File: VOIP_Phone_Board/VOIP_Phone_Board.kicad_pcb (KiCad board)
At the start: 2 copper layers, 65 x 56 mm, 25 parts, among them J1 69253-002LF, P1 Conn_02x20_Odd_Even, U1 PCM5102

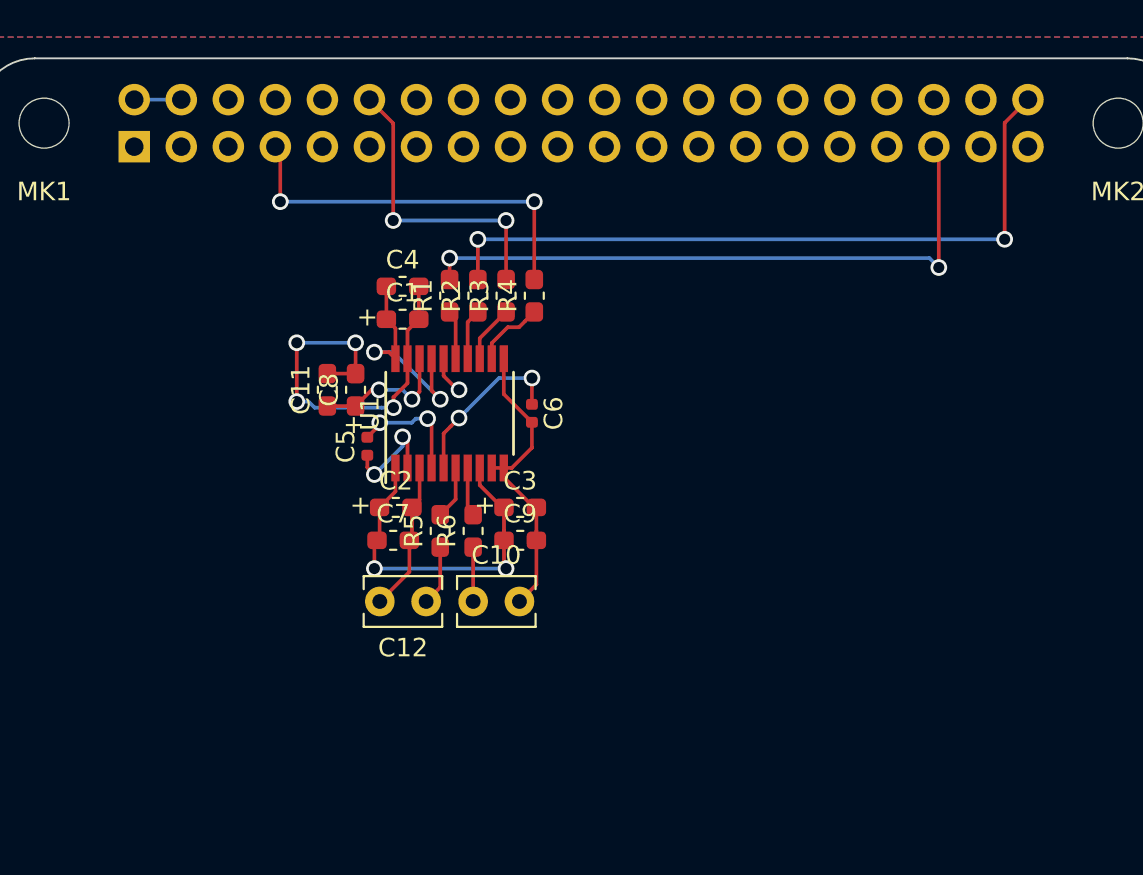
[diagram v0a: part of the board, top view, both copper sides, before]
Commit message: Completed audio input section.
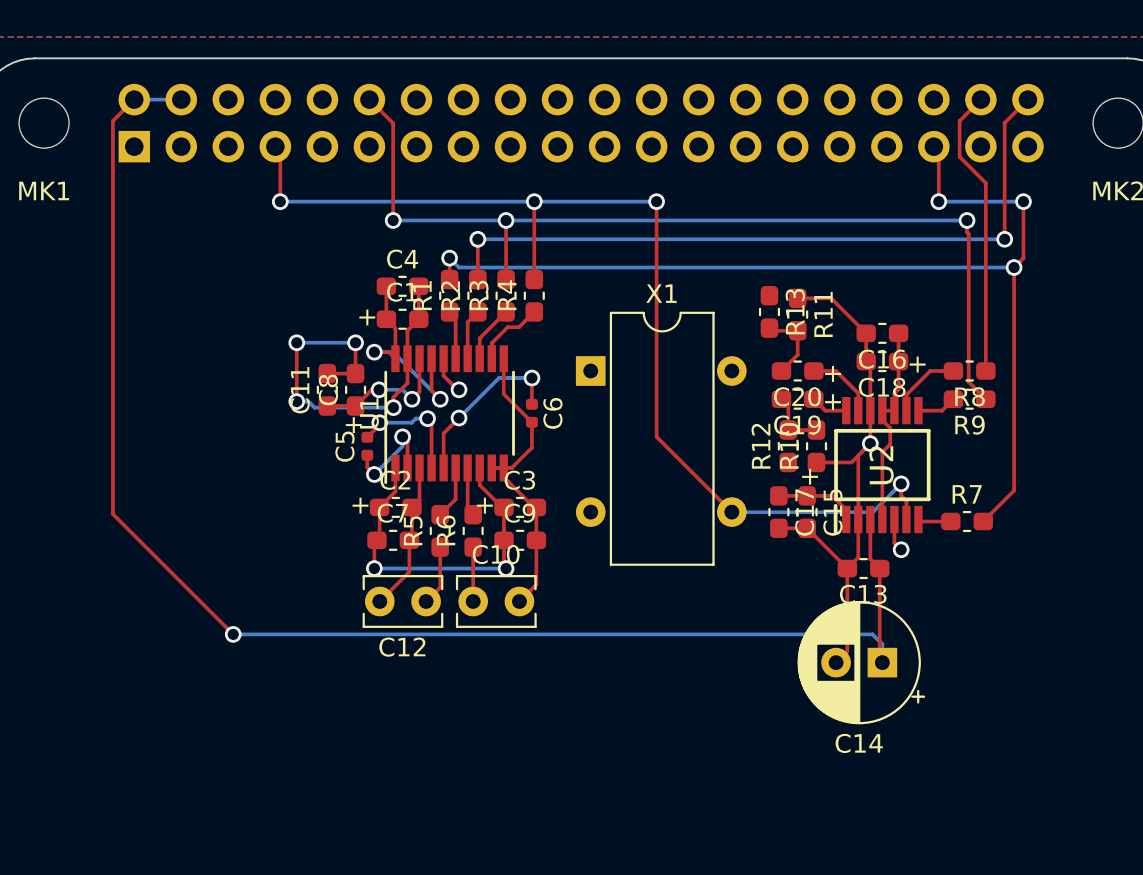
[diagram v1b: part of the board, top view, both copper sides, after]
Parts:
- added C13: .1uf, Capacitor_SMD:C_0603_1608Metric_Pad1.05x0.95mm_HandSolder, F.Cu at (247.8, 121.6)
- added C14: 47uf, Capacitor_THT:CP_Radial_D6.3mm_P2.50mm, F.Cu at (248.8, 126.6)
- added C15: 10uf, VOIP_Phone_Board:CP_0603_1608Metric_Pad1.05x0.95mm_HandSolder, F.Cu at (244.7, 118.5)
- added C16: .1uf, Capacitor_SMD:C_0603_1608Metric_Pad1.05x0.95mm_HandSolder, F.Cu at (248.8, 108.9)
- added C17: .1uf, Capacitor_SMD:C_0603_1608Metric_Pad1.05x0.95mm_HandSolder, F.Cu at (243.2, 118.5)
- added C18: 10uf, VOIP_Phone_Board:CP_0603_1608Metric_Pad1.05x0.95mm_HandSolder, F.Cu at (248.8, 110.4)
- added C19: 4.7uf, VOIP_Phone_Board:CP_0603_1608Metric_Pad1.05x0.95mm_HandSolder, F.Cu at (244.2, 112.4)
- added C20: 4.7uf, VOIP_Phone_Board:CP_0603_1608Metric_Pad1.05x0.95mm_HandSolder, F.Cu at (244.2, 110.9)
- added R10: 12K, Resistor_SMD:R_0603_1608Metric_Pad1.05x0.95mm_HandSolder, F.Cu at (245.2, 114.9)
- added R11: 12K, Resistor_SMD:R_0603_1608Metric_Pad1.05x0.95mm_HandSolder, F.Cu at (244.2, 107.8)
- added R12: 10K, Resistor_SMD:R_0603_1608Metric_Pad1.05x0.95mm_HandSolder, F.Cu at (243.7, 114.9)
- added R13: 10K, Resistor_SMD:R_0603_1608Metric_Pad1.05x0.95mm_HandSolder, F.Cu at (242.7, 107.7)
- added R7: 51, Resistor_SMD:R_0603_1608Metric_Pad1.05x0.95mm_HandSolder, F.Cu at (253.3, 119.0)
- added R8: 51, Resistor_SMD:R_0603_1608Metric_Pad1.05x0.95mm_HandSolder, F.Cu at (253.5, 110.9)
- added R9: 51, Resistor_SMD:R_0603_1608Metric_Pad1.05x0.95mm_HandSolder, F.Cu at (253.5, 112.4)
- added U2: PCM1808PW, VOIP_Phone_Board:SOP65P640X120-14N, F.Cu at (248.8, 116.0)
- added X1: SG-8002DC, Oscillator:Oscillator_SeikoEpson_SG-8002DC, F.Cu at (233.0, 110.9)
- C1: value CP1 -> 10uf
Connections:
- net Net-(C10-Pad1) renamed /Audio Subsystem/RightOut
- net Net-(C12-Pad1) renamed /Audio Subsystem/Leftout
- net Net-(J1-Pad1) renamed /Audio Subsystem/MIC_A(Black)
- net Net-(J1-Pad2) renamed /Audio Subsystem/SPKR_A(Red)
- net Net-(J1-Pad3) renamed /Audio Subsystem/SPKR_B(Green)
- net Net-(J1-Pad4) renamed /Audio Subsystem/MIC_B(Yellow)
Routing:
- net +5V: track 2.54 -> 78.9 mm, vias 0 -> 1
- net /Audio_MCLK: track 21.0 -> 57.9 mm, vias 2 -> 4
- net /DAP4_SCLK: track 16.3 -> 51.3 mm, vias 2 -> 3
- net GND: track 48.6 -> 81.5 mm, vias 5 -> 7
- net /DAP4_FS: track 34.4 -> 57.7 mm, vias 2 -> 4
- net /DAP4_DIN: track 0.00 -> 15.7 mm
- net +3V3: track 31.5 -> 42.7 mm
- net Net-(C15-Pad1): track 0.00 -> 4.47 mm
- net Net-(C20-Pad2): track 0.00 -> 4.12 mm
- net Net-(R8-Pad2): track 0.00 -> 3.92 mm
- net Net-(C20-Pad1): track 0.00 -> 3.83 mm
- net Net-(C19-Pad2): track 0.00 -> 3.34 mm
- net Net-(R9-Pad2): track 0.00 -> 2.14 mm
- net Net-(C19-Pad1): track 0.00 -> 2.00 mm
- net Net-(R7-Pad1): track 0.00 -> 1.79 mm

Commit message: Add keypad.
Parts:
- added J2: KeypadConnector, Connector_PinHeader_2.54mm:PinHeader_1x08_P2.54mm_Vertical, F.Cu at (204.1, 139.3)
- added KM1: KeypadMount, VOIP_Phone_Board:Keypad_mounting, F.Cu at (308.7, 124.6)
- moved J1 104.3 mm to (223.9, 143.9), turned to 90 degrees
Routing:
- net /GPIO5: track 0.00 -> 114.4 mm, vias 0 -> 2
- net /GPIO6: track 0.00 -> 106.4 mm, vias 0 -> 3
- net /GPIO16: track 0.00 -> 100.4 mm, vias 0 -> 2
- net /GPIO25(GEN6): track 0.00 -> 56.2 mm, vias 0 -> 1
- net /GPIO23(GEN4): track 0.00 -> 55.6 mm, vias 0 -> 2
- net /GPIO24(GEN5): track 0.00 -> 50.6 mm, vias 0 -> 3
- net /GPIO22(GEN3): track 0.00 -> 49.0 mm, vias 0 -> 3
- net GND: track 81.5 -> 130.4 mm, vias 7 -> 9
- net /GPIO17(GEN0): track 0.00 -> 47.8 mm, vias 0 -> 3
- net +3V3: track 42.7 -> 52.2 mm, vias 4 -> 5
- net +5V: track 78.9 -> 80.3 mm

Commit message: Add Hook Switch.
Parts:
- added J3: Hook, Connector_PinHeader_2.54mm:PinHeader_1x02_P2.54mm_Vertical, F.Cu at (262.5, 139.8)
- added R14: 10K, Resistor_SMD:R_0603_1608Metric_Pad1.05x0.95mm_HandSolder, F.Cu at (258.4, 139.8)
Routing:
- net /GPIO27(GEN2): track 0.00 -> 91.2 mm, vias 0 -> 4
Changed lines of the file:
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@@
     (thickness 1.6)
     (drawings 10)
-    (tracks 361)
+    (tracks 380)
     (zones 0)
-    (modules 44)
+    (modules 46)
     (nets 59)
   )
@@
     (uvia_dia 0.5)
     (uvia_drill 0.1)
+  )
+  (module Resistor_SMD:R_0603_1608Metric_Pad1.05x0.95mm_HandSolder (layer F.Cu)
+    (at 258.42 139.84)
+    (descr "Resistor SMD 0603 (1608 Metric), square (rectangular) end terminal, IPC_7351 nominal with elongated pad for handsoldering. (Body size source: http://www.tortai-tech.com/upload/download/2011102023233369053.pdf), generated with kicad-footprint-generator")
+    (tags "resistor handsolder")
+    (attr smd)
+    (fp_text reference R14 (at 0 -1.43) (layer F.SilkS)
+      (effects (font (size 1 1) (thickness 0.15)))
+    )
+    (fp_text value 10K (at 0 1.43) (layer F.Fab)
+      (effects (font (size 1 1) (thickness 0.15)))
+    )
+    (fp_line (start -0.8 0.4) (end -0.8 -0.4) (layer F.Fab) (width 0.1))
+    (fp_line (start -0.8 -0.4) (end 0.8 -0.4) (layer F.Fab) (width 0.1))
+    (fp_line (start 0.8 -0.4) (end 0.8 0.4) (layer F.Fab) (width 0.1))
+    (fp_line (start 0.8 0.4) (end -0.8 0.4) (layer F.Fab) (width 0.1))
+    (fp_line (start -0.171267 -0.51) (end 0.171267 -0.51) (layer F.SilkS) (width 0.12))
+    (fp_line (start -0.171267 0.51) (end 0.171267 0.51) (layer F.SilkS) (width 0.12))
+    (fp_line (start -1.65 0.73) (end -1.65 -0.73) (layer F.CrtYd) (width 0.05))
+    (fp_line (start -1.65 -0.73) (end 1.65 -0.73) (layer F.CrtYd) (width 0.05))
+    (fp_line (start 1.65 -0.73) (end 1.65 0.73) (layer F.CrtYd) (width 0.05))
+    (fp_line (start 1.65 0.73) (end -1.65 0.73) (layer F.CrtYd) (width 0.05))
+    (fp_text user %R (at 0 0) (layer F.Fab)
+      (effects (font (size 0.4 0.4) (thickness 0.06)))
+    )
+    (pad 1 smd roundrect (at -0.875 0) (size 1.05 0.95) (layers F.Cu F.Paste F.Mask) (roundrect_rratio 0.25)
+      (net 1 +3V3))
+    (pad 2 smd roundrect (at 0.875 0) (size 1.05 0.95) (layers F.Cu F.Paste F.Mask) (roundrect_rratio 0.25)
+      (net 14 "/GPIO27(GEN2)"))
+    (model ${KISYS3DMOD}/Resistor_SMD.3dshapes/R_0603_1608Metric.wrl
+      (at (xyz 0 0 0))
+      (scale (xyz 1 1 1))
+      (rotate (xyz 0 0 0))
+    )
   )
   (module Resistor_SMD:R_0603_1608Metric_Pad1.05x0.95mm_HandSolder (layer F.Cu)
@@
     (fp_line (start 34.29 38.1) (end -34.29 38.1) (layer F.SilkS) (width 0.4064))
     (fp_line (start -34.29 38.1) (end -34.29 -38.1) (layer F.SilkS) (width 0.4064))
+  )
+  (module Connector_PinHeader_2.54mm:PinHeader_1x02_P2.54mm_Vertical (layer F.Cu)
+    (at 262.484 139.84 180)
+    (descr "Through hole straight pin header, 1x02, 2.54mm pitch, single row")
+    (tags "Through hole pin header THT 1x02 2.54mm single row")
+    (fp_text reference J3 (at 0 -2.33) (layer F.SilkS)
+      (effects (font (size 1 1) (thickness 0.15)))
+    )
+    (fp_text value Hook (at 0 4.87) (layer F.Fab)
+      (effects (font (size 1 1) (thickness 0.15)))
+    )
+    (fp_line (start -0.635 -1.27) (end 1.27 -1.27) (layer F.Fab) (width 0.1))
+    (fp_line (start 1.27 -1.27) (end 1.27 3.81) (layer F.Fab) (width 0.1))
+    (fp_line (start 1.27 3.81) (end -1.27 3.81) (layer F.Fab) (width 0.1))
+    (fp_line (start -1.27 3.81) (end -1.27 -0.635) (layer F.Fab) (width 0.1))
+    (fp_line (start -1.27 -0.635) (end -0.635 -1.27) (layer F.Fab) (width 0.1))
+    (fp_line (start -1.33 3.87) (end 1.33 3.87) (layer F.SilkS) (width 0.12))
+    (fp_line (start -1.33 1.27) (end -1.33 3.87) (layer F.SilkS) (width 0.12))
+    (fp_line (start 1.33 1.27) (end 1.33 3.87) (layer F.SilkS) (width 0.12))
+    (fp_line (start -1.33 1.27) (end 1.33 1.27) (layer F.SilkS) (width 0.12))
+    (fp_line (start -1.33 0) (end -1.33 -1.33) (layer F.SilkS) (width 0.12))
+    (fp_line (start -1.33 -1.33) (end 0 -1.33) (layer F.SilkS) (width 0.12))
+    (fp_line (start -1.8 -1.8) (end -1.8 4.35) (layer F.CrtYd) (width 0.05))
+    (fp_line (start -1.8 4.35) (end 1.8 4.35) (layer F.CrtYd) (width 0.05))
+    (fp_line (start 1.8 4.35) (end 1.8 -1.8) (layer F.CrtYd) (width 0.05))
+    (fp_line (start 1.8 -1.8) (end -1.8 -1.8) (layer F.CrtYd) (width 0.05))
+    (fp_text user %R (at 0 1.27 90) (layer F.Fab)
+      (effects (font (size 1 1) (thickness 0.15)))
+    )
+    (pad 1 thru_hole rect (at 0 0 180) (size 1.7 1.7) (drill 1) (layers *.Cu *.Mask)
+      (net 14 "/GPIO27(GEN2)"))
+    (pad 2 thru_hole oval (at 0 2.54 180) (size 1.7 1.7) (drill 1) (layers *.Cu *.Mask)
+      (net 3 GND))
+    (model ${KISYS3DMOD}/Connector_PinHeader_2.54mm.3dshapes/PinHeader_1x02_P2.54mm_Vertical.wrl
+      (at (xyz 0 0 0))
+      (scale (xyz 1 1 1))
+      (rotate (xyz 0 0 0))
+    )
   )
   (gr_line (start 200 113) (end 200 131) (layer Edge.Cuts) (width 0.1))
@@
   (segment (start 205.588 130.188) (end 211.683998 130.188) (width 0.2) (layer B.Cu) (net 13))
   (segment (start 211.683998 130.188) (end 213.266001 128.605997) (width 0.2) (layer B.Cu) (net 13))
+  (via (at 259.436 137.3) (size 0.9) (drill 0.6) (layers F.Cu B.Cu) (net 14))
+  (via (at 217.78 135.268) (size 0.9) (drill 0.6) (layers F.Cu B.Cu) (net 14))
+  (segment (start 259.436 137.3) (end 257.404 135.268) (width 0.2) (layer B.Cu) (net 14))
+  (segment (start 257.404 135.268) (end 217.78 135.268) (width 0.2) (layer B.Cu) (net 14))
+  (segment (start 217.78 135.268) (end 217.78 133.744) (width 0.2) (layer F.Cu) (net 14))
+  (via (at 217.78 104.788) (size 0.9) (drill 0.6) (layers F.Cu B.Cu) (net 14))
+  (segment (start 217.895001 104.903001) (end 217.78 104.788) (width 0.2) (layer F.Cu) (net 14))
+  (segment (start 217.78 133.744) (end 217.895001 133.628999) (width 0.2) (layer F.Cu) (net 14))
+  (segment (start 217.895001 133.628999) (end 217.895001 104.903001) (width 0.2) (layer F.Cu) (net 14))
+  (via (at 223.368 103.772) (size 0.9) (drill 0.6) (layers F.Cu B.Cu) (net 14))
+  (segment (start 217.78 104.788) (end 222.352 104.788) (width 0.2) (layer B.Cu) (net 14))
+  (segment (start 222.352 104.788) (end 223.368 103.772) (width 0.2) (layer B.Cu) (net 14))
+  (segment (start 223.368 99.012) (end 223.61 98.77) (width 0.2) (layer F.Cu) (net 14))
+  (segment (start 223.368 103.772) (end 223.368 99.012) (width 0.2) (layer F.Cu) (net 14))
+  (segment (start 259.436 139.699) (end 259.295 139.84) (width 0.2) (layer F.Cu) (net 14))
+  (segment (start 259.436 137.3) (end 259.436 139.699) (width 0.2) (layer F.Cu) (net 14))
+  (segment (start 259.436 137.842) (end 259.436 137.3) (width 0.2) (layer B.Cu) (net 14))
+  (segment (start 261.434 139.84) (end 259.436 137.842) (width 0.2) (layer B.Cu) (net 14))
+  (segment (start 262.484 139.84) (end 261.434 139.84) (width 0.2) (layer B.Cu) (net 14))
   (via (at 211.176 105.804) (size 0.9) (drill 0.6) (layers F.Cu B.Cu) (net 15))
   (via (at 225.4 103.687997) (size 0.9) (drill 0.6) (layers F.Cu B.Cu) (net 15))

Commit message: Complete all I/O and connectors.
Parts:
- removed KM1: KeypadMount, VOIP_Phone_Board:Keypad_mounting
- added J4: Hook, Connector_PinHeader_2.54mm:PinHeader_1x02_P2.54mm_Vertical, F.Cu at (262.5, 139.8)
- added J5: Speaker, Connector_PinHeader_2.54mm:PinHeader_1x02_P2.54mm_Vertical, F.Cu at (209.7, 138.8)
- added J6: Microphone, Connector_PinHeader_2.54mm:PinHeader_1x02_P2.54mm_Vertical, F.Cu at (209.7, 143.4)
- added J7: Control Buttons, Connector_PinHeader_2.54mm:PinHeader_1x05_P2.54mm_Vertical, F.Cu at (232.3, 142.4)
- added R15: 10K, Resistor_SMD:R_0603_1608Metric_Pad1.05x0.95mm_HandSolder, F.Cu at (240.1, 146.6)
- added R16: 10K, Resistor_SMD:R_0603_1608Metric_Pad1.05x0.95mm_HandSolder, F.Cu at (237.6, 146.6)
- added R17: 10K, Resistor_SMD:R_0603_1608Metric_Pad1.05x0.95mm_HandSolder, F.Cu at (234.5, 146.4)
- added R18: 10K, Resistor_SMD:R_0603_1608Metric_Pad1.05x0.95mm_HandSolder, F.Cu at (232.5, 146.6)
- J1: value 69253-002LF -> Headset; footprint VOIP_Phone_Board:69253002LF -> Connector_PinHeader_2.54mm:PinHeader_1x04_P2.54mm_Vertical
- J2: value KeypadConnector -> Display; footprint Connector_PinHeader_2.54mm:PinHeader_1x08_P2.54mm_Vertical -> Connector_PinHeader_2.54mm:PinHeader_1x06_P2.54mm_Vertical
- J3: value Hook -> KeypadConnector; footprint Connector_PinHeader_2.54mm:PinHeader_1x02_P2.54mm_Vertical -> Connector_PinHeader_2.54mm:PinHeader_1x08_P2.54mm_Vertical
- moved J3 58.9 mm to (203.6, 139.3)
- moved J2 34.5 mm to (203.6, 104.8), turned to 0 degrees
- moved J1 7.13 mm to (216.8, 143.4)
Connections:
- J2 pad 1: /GPIO5 -> /GPIO2(SDA1)
- J2 pad 2: /GPIO6 -> /GPIO3(SCL1)
- J2 pad 3: /GPIO16 -> /GPIO26
- J2 pad 4: /GPIO17(GEN0) -> GND
- J2 pad 5: /GPIO22(GEN3) -> +3V3
- J2 pad 6: /GPIO23(GEN4) -> Net-(J2-Pad6)
- J3 pad 1: /GPIO27(GEN2) -> /GPIO5
- J3 pad 2: GND -> /GPIO6
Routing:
- net /GPIO26: track 0.00 -> 62.7 mm, vias 0 -> 1
- net /GPIO8(SPI0_CE_N): track 0.00 -> 55.2 mm, vias 0 -> 2
- net +3V3: track 52.2 -> 102.6 mm, vias 5 -> 9
- net /GPIO11(SPI0_SCK): track 0.00 -> 48.2 mm
- net /GPIO10(SPI0_MOSI): track 0.00 -> 48.1 mm
- net /GPIO9(SPI0_MISO): track 0.00 -> 47.7 mm
- net /GPIO3(SCL1): track 0.00 -> 17.7 mm, vias 0 -> 1
- net /GPIO2(SDA1): track 0.00 -> 13.2 mm, vias 0 -> 1
- net GND: track 130.4 -> 139.0 mm
- net /DAP4_FS: track 57.7 -> 61.9 mm
- net /DAP4_DOUT: track 38.7 -> 41.1 mm
- net /GPIO16: track 100.4 -> 99.6 mm
- net /GPIO17(GEN0): track 47.8 -> 47.1 mm
